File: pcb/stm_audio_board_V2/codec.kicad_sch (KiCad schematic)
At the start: 0 parts

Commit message: ad1939 symbol is finished
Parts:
- added U11: ~, symbol codec:AD1939
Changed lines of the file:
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@@
 (kicad_sch (version 20230121) (generator eeschema)
   (paper "A4")
+  (symbol (lib_name "AD1939_1") (lib_id "codec:AD1939") (at 60.96 27.94 0) (unit 1)
+    (in_bom yes) (on_board yes) (dnp no) (fields_autoplaced)
+    (property "Reference" "U11" (at 68.58 29.21 0)
+      (effects (font (size 1.27 1.27)))
+    )
+    (property "Value" "~" (at 60.96 27.94 0)
+      (effects (font (size 1.27 1.27)))
+    )
+    (property "Footprint" "" (at 60.96 27.94 0)
+      (effects (font (size 1.27 1.27)) hide)
+    )
+    (property "Datasheet" "" (at 60.96 27.94 0)
+      (effects (font (size 1.27 1.27)) hide)
+    )
+    (pin "10")
+    (pin "11")
+    (pin "12")
+    (pin "13")
+    (pin "14")
+    (pin "15")
+    (pin "18")
+    (pin "19")
+    (pin "2")
+    (pin "20")
+    (pin "21")
+    (pin "22")
+    (pin "26")
+    (pin "27")
+    (pin "28")
+    (pin "29")
+    (pin "3")
+    (pin "30")
+    (pin "31")
+    (pin "34")
+    (pin "35")
+    (pin "37")
+    (pin "38")
+    (pin "38")
+    (pin "39")
+    (pin "40")
+    (pin "41")
+    (pin "42")
+    (pin "43")
+    (pin "47")
+    (pin "52")
+    (pin "53")
+    (pin "54")
+    (pin "55")
+    (pin "56")
+    (pin "57")
+    (pin "58")
+    (pin "59")
+    (pin "6")
+    (pin "60")
+    (pin "61")
+    (pin "7")
+    (pin "8")
+    (pin "9")
+    (pin "1")
+    (pin "16")
+    (pin "17")
+    (pin "23")
+    (pin "24")
+    (pin "25")
+    (pin "32")
+    (pin "33")
+    (pin "4")
+    (pin "44")
+    (pin "45")
+    (pin "46")
+    (pin "48")
+    (pin "49")
+    (pin "5")
+    (pin "50")
+    (pin "51")
+    (pin "62")
+    (pin "63")
+    (pin "64")
+    (instances
+      (project "stm_audio_board_V2"
+        (path "/6997cf63-2615-4e49-9471-e7da1b6bae71/8744407a-1e34-4228-b7c6-9fdc39f322d4"
+          (reference "U11") (unit 1)
+        )
+      )
+    )
+  )
 )

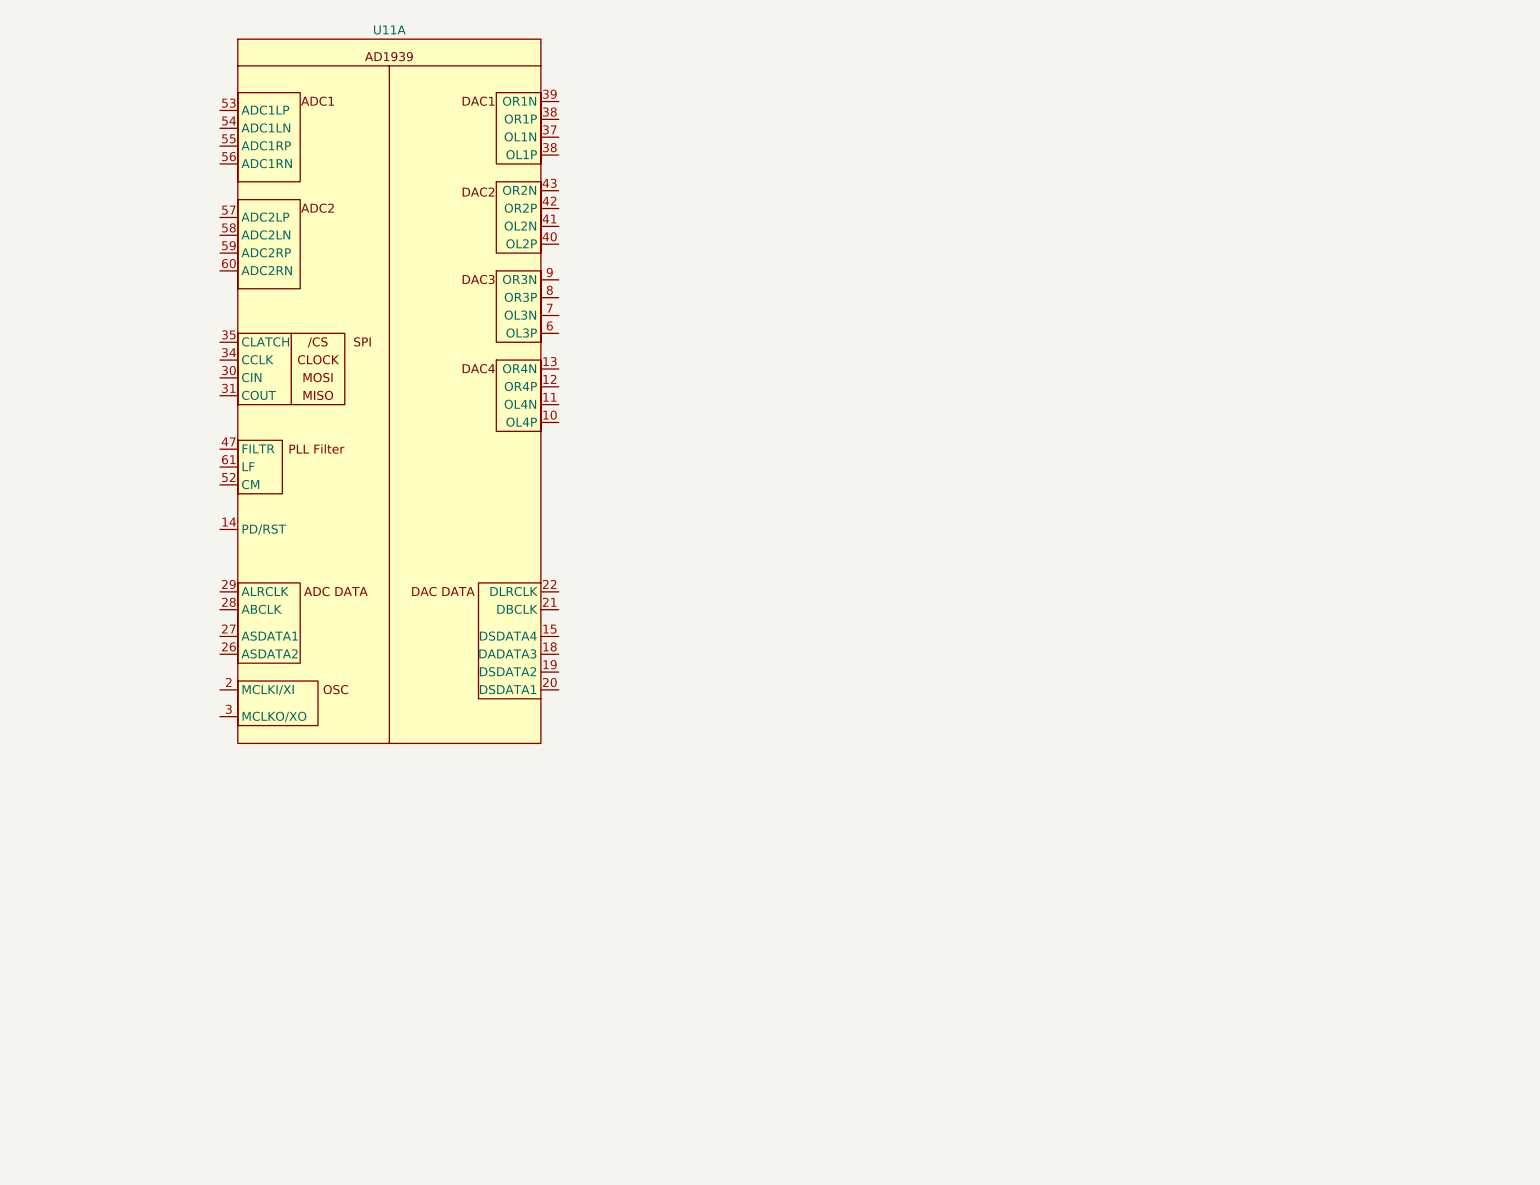
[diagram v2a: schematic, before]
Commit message: input and output stage reworked in sim and in schematic, power filtering is changed, further calculations needed
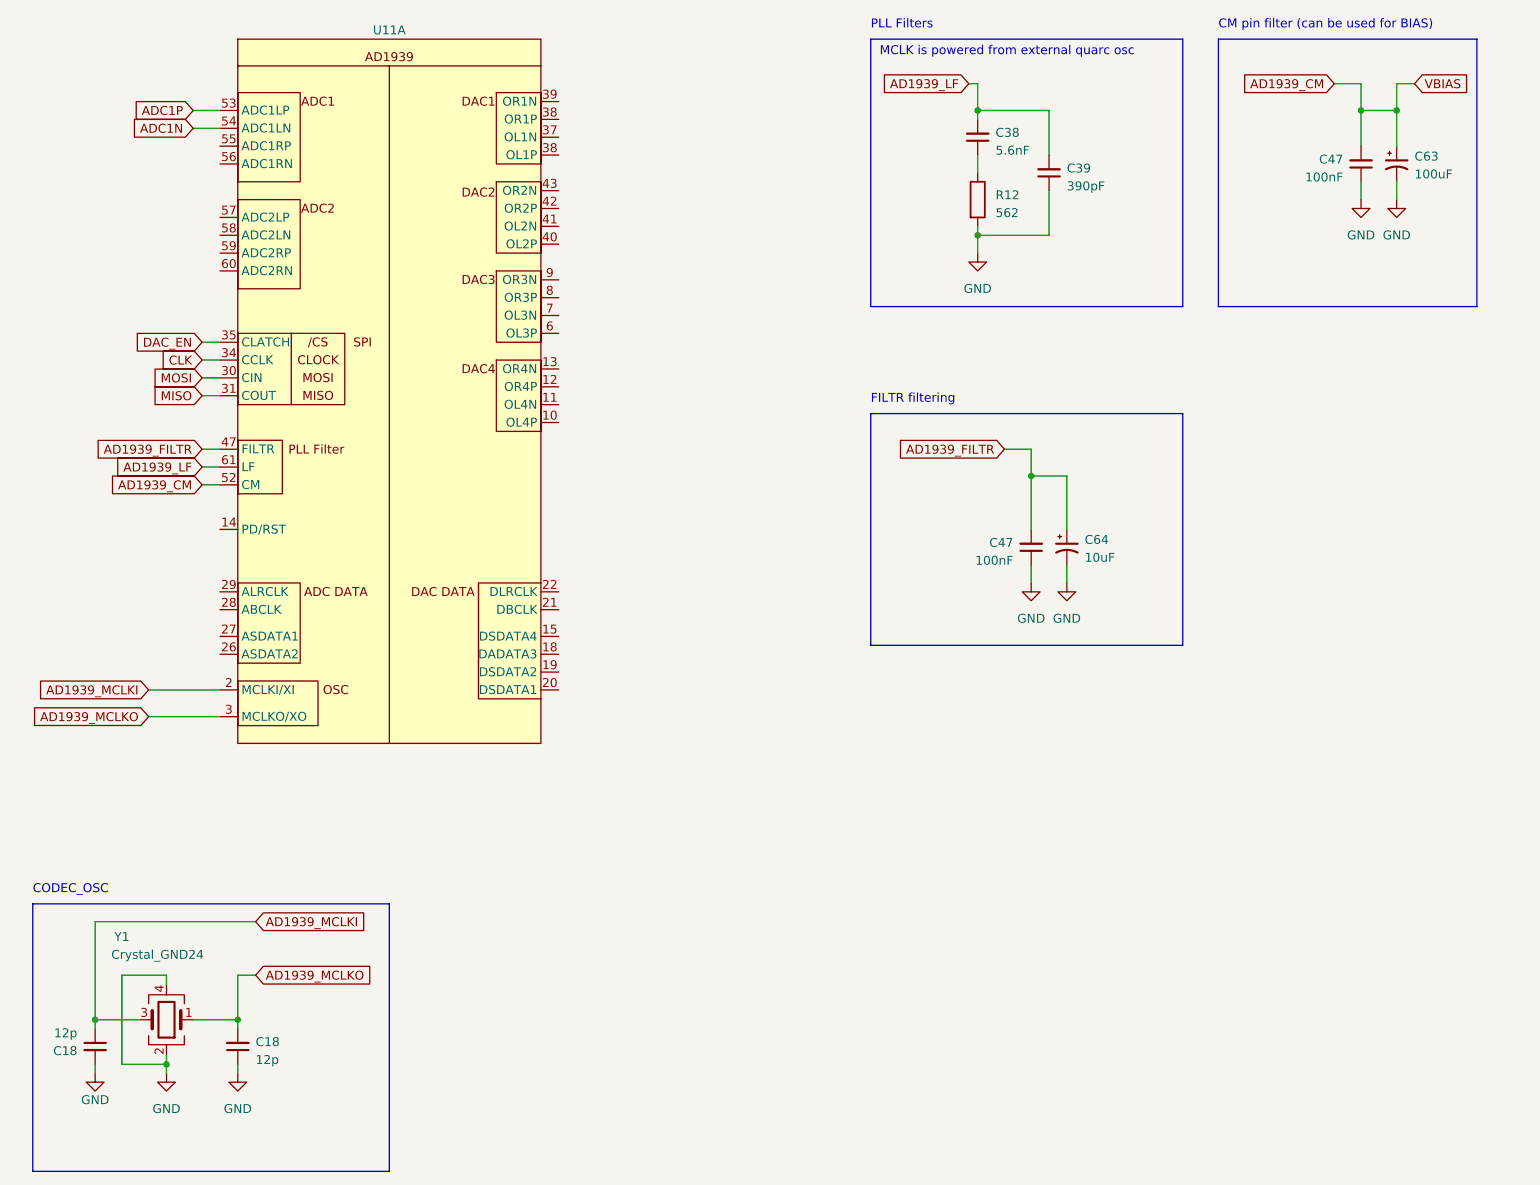
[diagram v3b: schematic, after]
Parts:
- added C18 (x2): 12p, Capacitor_SMD:C_0603_1608Metric_Pad1.08x0.95mm_HandSolder, symbol Device:C_Small
- added C38: 5.6nF, Capacitor_SMD:C_0603_1608Metric_Pad1.08x0.95mm_HandSolder, symbol Device:C_Small
- added C39: 390pF, Capacitor_SMD:C_0603_1608Metric_Pad1.08x0.95mm_HandSolder, symbol Device:C_Small
- added C47 (x2): 100nF, Capacitor_SMD:C_0603_1608Metric_Pad1.08x0.95mm_HandSolder, symbol Device:C_Small
- added C63: 100uF, Capacitor_SMD:C_1210_3225Metric_Pad1.33x2.70mm_HandSolder, symbol Device:C_Polarized_Small_US
- added C64: 10uF, Capacitor_SMD:C_1210_3225Metric_Pad1.33x2.70mm_HandSolder, symbol Device:C_Polarized_Small_US
- added R12: 562, Resistor_SMD:R_0805_2012Metric_Pad1.20x1.40mm_HandSolder, symbol Device:R
- added Y1: Crystal_GND24, Crystal:Crystal_SMD_5032-4Pin_5.0x3.2mm, symbol Device:Crystal_GND24
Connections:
- net AD1939_MCLKI: now reaches U11.2 (MCLKI/XI)
- net AD1939_MCLKI: now also C18.1, Y1.3
- net AD1939_MCLKO: now reaches U11.3 (MCLKO/XO)
- net AD1939_MCLKO: now also C18.2, Y1.1
- net MOSI: now reaches U11.30 (CIN)
- net MISO: now reaches U11.31 (COUT)
- net CLK: now reaches U11.34 (CCLK)
- net DAC_EN: now reaches U11.35 (CLATCH)
- net AD1939_FILTR: now reaches U11.47 (FILTR)
- net AD1939_FILTR: now also C47.2, C64.1
- net AD1939_CM: now reaches U11.52 (CM)
- net AD1939_CM: now also C47.2, C63.1
- net ADC1P: now reaches U11.53 (ADC1LP)
- net ADC1N: now reaches U11.54 (ADC1LN)
- net AD1939_LF: now reaches U11.61 (LF)
- net AD1939_LF: now also C38.2, C39.2
- new net: C38.1, R12.1
- new net GND: C18.1, C18.2, C39.1, C47.1, C47.1, C63.2, C64.2, R12.2, Y1.2, Y1.4
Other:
- note added: "CM pin filter (can be used for BIAS)"
- note added: "CODEC_OSC"
- note added: "FILTR filtering"
- note added: "MCLK is powered from external quarc osc"
- note added: "PLL Filters"
